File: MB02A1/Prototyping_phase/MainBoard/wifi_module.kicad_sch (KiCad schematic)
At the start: 1 part, among them U9 WEMOS_D1_mini

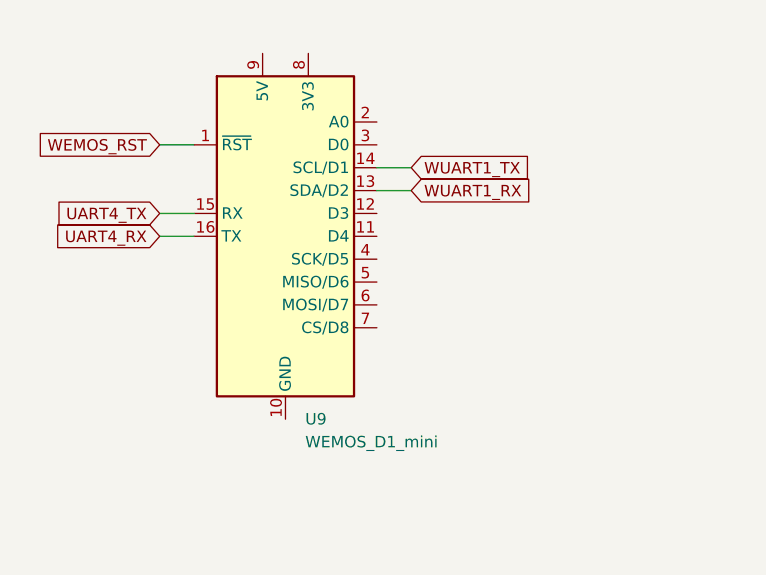
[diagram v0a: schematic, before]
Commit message: Datasheets added, design updated.
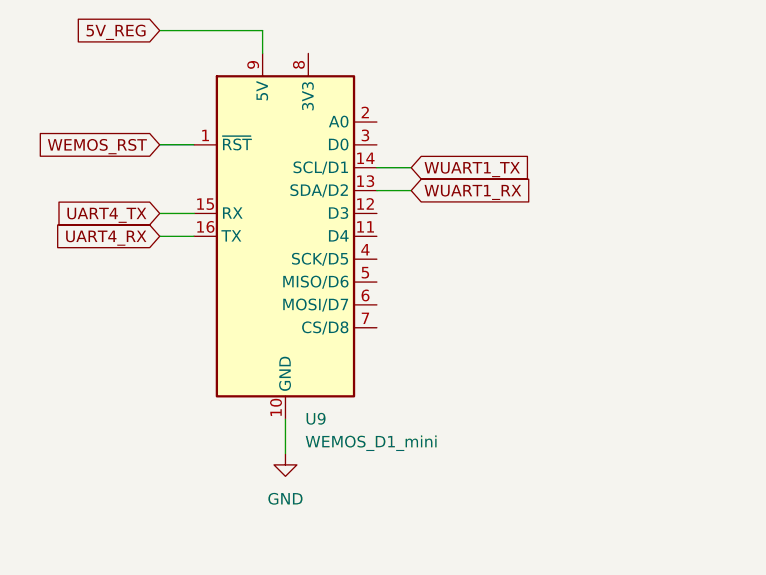
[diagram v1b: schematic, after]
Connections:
- net GND: now reaches U9.10 (GND)
- net 5V_REG: now reaches U9.9 (5V)
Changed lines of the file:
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@@
+	(wire
+		(pts
+			(xy 127 66.04) (xy 138.43 66.04)
+		)
+		(stroke
+			(width 0)
+			(type default)
+		)
+	)
 	(wire
 		(pts
@@
 	(wire
 		(pts
+			(xy 140.97 109.22) (xy 140.97 113.03)
+		)
+		(stroke
+			(width 0)
+			(type default)
+		)
+	)
+	(wire
+		(pts
+			(xy 138.43 66.04) (xy 138.43 68.58)
+		)
+		(stroke
+			(width 0)
+			(type default)
+		)
+	)
+	(wire
+		(pts
 			(xy 151.13 83.82) (xy 154.94 83.82)
 		)
@@
 		)
 	)
+	(global_label "5V_REG"
+		(shape input)
+		(at 127 66.04 180)
+		(fields_autoplaced yes)
+		(effects
+			(font
+				(size 1.27 1.27)
+			)
+			(justify right)
+		)
+		(property "Intersheetrefs" "${INTERSHEET_REFS}"
+			(at 117.0601 66.04 0)
+			(effects
+				(font
+					(size 1.27 1.27)
+				)
+				(justify right)
+				(hide yes)
+			)
+		)
+	)
 	(global_label "WUART1_TX"
 		(shape input)
@@
 			)
 		)
+	)
+	(symbol
+		(lib_id "power:GND")
+		(at 140.97 113.03 0)
+		(unit 1)
+		(exclude_from_sim no)
+		(in_bom yes)
+		(on_board yes)
+		(dnp no)
+		(fields_autoplaced yes)
+		(property "Reference" "#PWR027"
+			(at 140.97 119.38 0)
+			(effects
+				(font
+					(size 1.27 1.27)
+				)
+				(hide yes)
+			)
+		)
+		(property "Value" "GND"
+			(at 140.97 118.11 0)
+			(effects
+				(font
+					(size 1.27 1.27)
+				)
+			)
+		)
+		(property "Footprint" ""
+			(at 140.97 113.03 0)
+			(effects
+				(font
+					(size 1.27 1.27)
+				)
+				(hide yes)
+			)
+		)
+		(property "Datasheet" ""
+			(at 140.97 113.03 0)
+			(effects
+				(font
+					(size 1.27 1.27)
+				)
+				(hide yes)
+			)
+		)
+		(property "Description" "Power symbol creates a global label with name \"GND\" , ground"
+			(at 140.97 113.03 0)
+			(effects
+				(font
+					(size 1.27 1.27)
+				)
+				(hide yes)
+			)
+		)
+		(pin "1"
+		)
+		(instances
+			(project "mb02a1"
+				(path "/ee4e0941-1c36-4545-8b22-b979d73b3a97/27869566-fa24-4e10-9012-10a05996ae4f"
+					(reference "#PWR027")
+					(unit 1)
+				)
+			)
+		)

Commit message: Design update, production preparation.
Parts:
- added D13, D14, D15: LED, LED_SMD:LED_1206_3216Metric, symbol Device:LED
- added R24, R25, R26: 1k5, Resistor_SMD:R_0805_2012Metric, symbol Device:R
- renumbered U9 to U10
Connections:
- net GND: now also R24.2, R25.2, R26.2
- net at U10.4 (SCK/D5): now also D15.2 (A)
- net at U10.5 (MISO/D6): now also D14.2 (A)
- net at U10.6 (MOSI/D7): now also D13.2 (A)
- new net: D15.1 (K), R26.1
- new net: D14.1 (K), R25.1
- new net: D13.1 (K), R24.1
